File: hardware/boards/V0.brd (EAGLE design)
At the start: 61 parts, among them IC2 TPS6300, J1 SJ-43515TS-SMT, J2 HIROSE_DM3BT-DSF-PEJSHIROSE_D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, J3 MOLEX_105450-0101MOLEX_105450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, Q1 MC-306, Q2 ON_SEMI_MMBT5551LT1GON_SEMI_M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, U1 VS1053-L, X1 PG203J, X3 FH12-45S-0.5SH

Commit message: checkpoint: USB
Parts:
- added C21: 0.1uF, rcl:C0805K
- added C22, C24: 4.7uF, rcl:C/6032-28R
- added C23, C25: 0.1uF, rcl:C/6032-28R
- added CENTER_SW, DOWN_SW, LEFT_SW, RIGHT_SW, UP_SW: E-SWITCH_TL3315NF160QE-SWITCH_TL3315NF160Q_0_0, E-Switch-TL3315NF160Q:E-SWITCH_TL3315NF160Q_0
- added D10, D8, D9: ON_SEMICONDUCTOR_ESD5Z5.0T1GON_SEMICONDUCTOR_ESD5Z5.0T1G_0_0, ESD-Diode_On-Semi-ESD5Z5.0T1G:ON_SEMICONDUCTOR_ESD5Z5.0T1G_0
- added D3, D4, D5, D6, D7: (no value), adafruit:SOD-523
- added R19, R25, R33: 5k, rcl:R0805
- added R20: 15k, rcl:R0805
- added R21: 35k, rcl:R0805
- added R22: 75k, rcl:R0805
- added R23: 155k, rcl:R0805
- added R24: 50k, rcl:R0805
- added R26, R32: 10k, rcl:R0805
- added R27, R28: 5.1k, rcl:R0805
- added R29: 22.1k, rcl:R0805
- added R30: 47.5k, rcl:R0805
- added R31: 1k, rcl:R0805
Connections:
- removed net 1_GND: J3.A1
- removed net 1_VBUS: J3.A4
- removed net 2_GND: J3.A12
- removed net 2_VBUS: J3.A9
- removed net 3_GND: J3.B1
- removed net 3_VBUS: J3.B4
- removed net 4_GND: J3.B12
- removed net 4_VBUS: J3.B9
- removed net VDD: JL.P$6
- removed net VREGIN: JL.P$7
- new net BUTTON_ADC: R19.1, R20.1, R21.1, R22.1, R23.1, R25.2
- new net BUTTON_DIN: C21.2, R24.2
- new net CP_VDD: C24.+, C25.+, JL.P$6, R31.2
- new net N$16: D3.A, LEFT_SW.4, LEFT_SW.4-2, R19.2
- new net N$24: D4.A, R20.2, UP_SW.4, UP_SW.4-2
- new net N$28: D5.A, R21.2, RIGHT_SW.4, RIGHT_SW.4-2
- new net N$29: D6.A, DOWN_SW.4, DOWN_SW.4-2, R22.2
- new net N$32: D3.K, D4.K, D5.K, D6.K, D7.K, R24.1, R26.2
- new net N$49: CENTER_SW.4, CENTER_SW.4-2, D7.A, R23.2
- new net N$50: J3.A5, R27.1
- new net N$51: J3.B5, R28.1
- new net N$52: JL.P$8, R29.1, R30.2
- new net N$53: JL.P$9, R31.1
- new net USB_D+: D9.1, J3.A6, J3.B6, JL.P$4
- new net USB_D-: D8.1, J3.A7, J3.B7, JL.P$5
- new net VBAT_ADC_IN: R32.2, R33.1
- new net VBUS: D10.1, J3.A4, J3.A9, J3.B4, J3.B9, R29.2
- net GND: now also C22.-, C23.-, C24.-, C25.-, D10.2, D8.2, D9.2, J3.1, J3.2, J3.3, J3.4, J3.A1, J3.A12, J3.B1, J3.B12, R25.1, R26.1, R27.2, R28.2, R30.1, R32.1
- net V3P3: now also C21.1, CENTER_SW.2, CENTER_SW.2-2, D1.2, DOWN_SW.2, DOWN_SW.2-2, LEFT_SW.2, LEFT_SW.2-2, RIGHT_SW.2, RIGHT_SW.2-2, UP_SW.2, UP_SW.2-2
- net VBAT: now also C22.+, C23.+, JL.P$7, R33.2

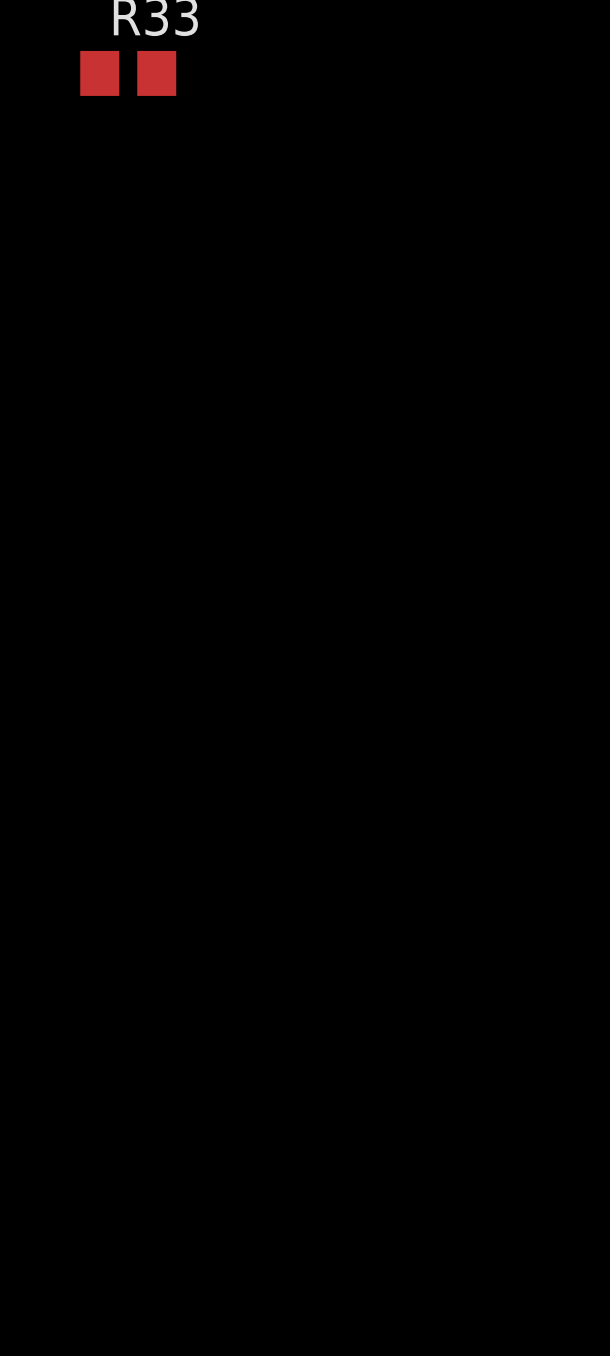
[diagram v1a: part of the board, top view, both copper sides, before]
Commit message: checkpoint: LED, battery voltage circuit, charge IC, half of the CP2102N
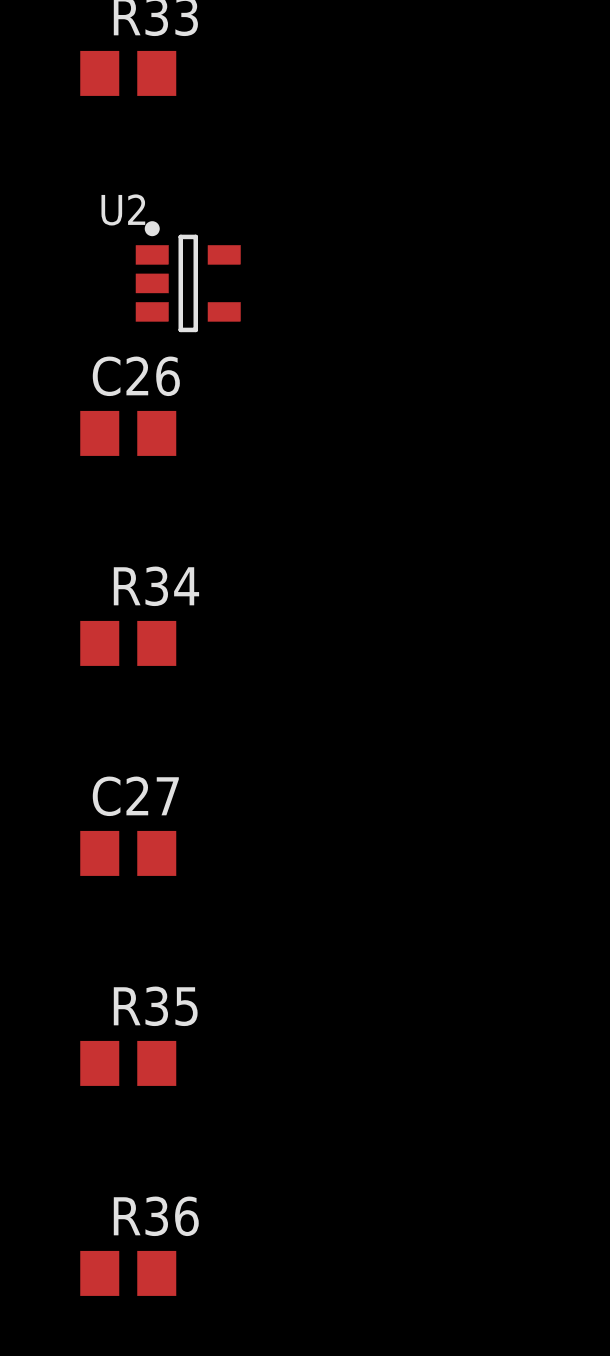
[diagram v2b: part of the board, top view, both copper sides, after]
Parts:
- added C26, C27: 4.7uF, rcl:C0805
- added R34: 2k, rcl:R0805
- added R35: 100, rcl:R0805
- added R36: (no value), rcl:R0805
- added U2: MICROCHIP_MCP73831T-2ATI-OTMICROCHIP_MCP73831T-2ATI-OT_0_1, Microchip-MCP73831T-2ATI:MICROCHIP_MCP73831T-2ATI-OT_1
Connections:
- new net BLUE_LED_CATH: D1.1
- new net GREEN_LED_CATH: R36.2
- new net N$54: R34.1, U2.5
- new net N$55: D1.3, R35.1
- new net N$56: D1.4, R36.1
- new net RED_LED_CATH: R35.2, U2.1
- net GND: now also C26.2, C27.2, R34.2, U2.2
- net VBAT: now also C26.1, U2.3
- net VBUS: now also C27.1, U2.4
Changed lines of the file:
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@@
 <attribute name="VALUE" x="-36.635" y="-531.54" size="1.27" layer="27"/>
+</element>
+<element name="U2" library="Microchip-MCP73831T-2ATI" package="MICROCHIP_MCP73831T-2ATI-OT_1" value="MICROCHIP_MCP73831T-2ATI-OTMICROCHIP_MCP73831T-2ATI-OT_0_1" x="-34" y="-536" smashed="yes">
+<attribute name="CIIVA_IDS" value="961386" x="-34" y="-536" size="1.778" layer="27" display="off"/>
+<attribute name="CODE__IPC" value="SOT23-5" x="-34" y="-536" size="1.778" layer="27" display="off"/>
+<attribute name="DATASHEET_VERSION" value="revE, Sep-2008" x="-34" y="-536" size="1.778" layer="27" display="off"/>
+<attribute name="FOOTPRINT_VARIANT_NAME_0" value="Level C" x="-34" y="-536" size="1.778" layer="27" display="off"/>
+<attribute name="FOOTPRINT_VARIANT_NAME_1" value="Level B" x="-34" y="-536" size="1.778" layer="27" display="off"/>
+<attribute name="FOOTPRINT_VARIANT_NAME_2" value="Level A" x="-34" y="-536" size="1.778" layer="27" display="off"/>
+<attribute name="IMPORTED" value="yes" x="-34" y="-536" size="1.778" layer="27" display="off"/>
+<attribute name="IMPORTED_FROM" value="vault" x="-34" y="-536" size="1.778" layer="27" display="off"/>
+<attribute name="IMPORT_TS" value="1521858219" x="-34" y="-536" size="1.778" layer="27" display="off"/>
+<attribute name="MF" value="Microchip" x="-34" y="-536" size="1.778" layer="27" display="off"/>
+<attribute name="MPN" value="MCP73831T-2ATI/OT" x="-34" y="-536" size="1.778" layer="27" display="off"/>
+<attribute name="NAME" x="-37" y="-534.05" size="1" layer="25"/>
+<attribute name="PACKAGE" value="SOT-23-OT5" x="-34" y="-536" size="1.778" layer="27" display="off"/>
+<attribute name="PACKAGE_DESCRIPTION" value="5-Lead Plastic Small Outline Transistor (OT) [SOT-23]" x="-34" y="-536" size="1.778" layer="27" display="off"/>
+<attribute name="PACKAGE_VERSION" value="revBB, Aug-2009" x="-34" y="-536" size="1.778" layer="27" display="off"/>
+<attribute name="PREFIX" value="U" x="-34" y="-536" size="1.778" layer="27" display="off"/>
+<attribute name="RELEASE_DATE" value="1300334172" x="-34" y="-536" size="1.778" layer="27" display="off"/>
+<attribute name="VAULT_GUID" value="2E16BB74-376E-4BA5-8468-379BB32F6F4F" x="-34" y="-536" size="1.778" layer="27" display="off"/>
+<attribute name="VAULT_REVISION" value="08CA403F-6CAA-4AD2-9BA5-F14A59377F17" x="-34" y="-536" size="1.778" layer="27" display="off"/>
+</element>
+<element name="C26" library="rcl" library_urn="urn:adsk.eagle:library:334" package="C0805" package3d_urn="urn:adsk.eagle:package:23617/2" value="4.7uF" x="-36" y="-541" smashed="yes">
+<attribute name="NAME" x="-37.27" y="-539.73" size="1.27" layer="25"/>
+<attribute name="SPICEPREFIX" value="C" x="-36" y="-541" size="1.778" layer="27" display="off"/>
+<attribute name="VALUE" x="-37.27" y="-543.54" size="1.27" layer="27"/>
+</element>
+<element name="R34" library="rcl" library_urn="urn:adsk.eagle:library:334" package="R0805" package3d_urn="urn:adsk.eagle:package:23553/2" value="2k" x="-36" y="-548" smashed="yes">
+<attribute name="NAME" x="-36.635" y="-546.73" size="1.27" layer="25"/>
+<attribute name="SPICEPREFIX" value="R" x="-36" y="-548" size="1.778" layer="27" display="off"/>
+<attribute name="VALUE" x="-36.635" y="-550.54" size="1.27" layer="27"/>
+</element>
+<element name="C27" library="rcl" library_urn="urn:adsk.eagle:library:334" package="C0805" package3d_urn="urn:adsk.eagle:package:23617/2" value="4.7uF" x="-36" y="-555" smashed="yes">
+<attribute name="NAME" x="-37.27" y="-553.73" size="1.27" layer="25"/>
+<attribute name="SPICEPREFIX" value="C" x="-36" y="-555" size="1.778" layer="27" display="off"/>
+<attribute name="VALUE" x="-37.27" y="-557.54" size="1.27" layer="27"/>
+</element>
+<element name="R35" library="rcl" library_urn="urn:adsk.eagle:library:334" package="R0805" package3d_urn="urn:adsk.eagle:package:23553/2" value="100" x="-36" y="-562" smashed="yes">
+<attribute name="NAME" x="-36.635" y="-560.73" size="1.27" layer="25"/>
+<attribute name="SPICEPREFIX" value="R" x="-36" y="-562" size="1.778" layer="27" display="off"/>
+<attribute name="VALUE" x="-36.635" y="-564.54" size="1.27" layer="27"/>
+</element>
+<element name="R36" library="rcl" library_urn="urn:adsk.eagle:library:334" package="R0805" package3d_urn="urn:adsk.eagle:package:23553/2" value="" x="-36" y="-569" smashed="yes">
+<attribute name="NAME" x="-36.635" y="-567.73" size="1.27" layer="25"/>
+<attribute name="SPICEPREFIX" value="R" x="-36" y="-569" size="1.778" layer="27" display="off"/>
+<attribute name="VALUE" x="-36.635" y="-571.54" size="1.27" layer="27"/>
 </element>
 </elements>
@@
 <contactref element="C25" pad="-"/>
 <contactref element="R32" pad="1"/>
+<contactref element="C26" pad="2"/>
+<contactref element="U2" pad="2"/>
+<contactref element="R34" pad="2"/>
+<contactref element="C27" pad="2"/>
 <wire x1="-21.275" y1="-222.175" x2="-28.675" y2="-222.175" width="0" layer="19" extent="1-1"/>
 <wire x1="-24.075" y1="-200.0822" x2="-21.275" y2="-222.175" width="0" layer="19" extent="1-1"/>
@@
 <wire x1="-36.525" y1="-517" x2="-36.525" y2="-509" width="0" layer="19" extent="1-1"/>
 <wire x1="-36.95" y1="-524" x2="-36.525" y2="-517" width="0" layer="19" extent="1-1"/>
+<wire x1="-35.2" y1="-536" x2="-36.95" y2="-524" width="0" layer="19" extent="1-1"/>
+<wire x1="-35.05" y1="-541" x2="-35.2" y2="-536" width="0" layer="19" extent="1-1"/>
+<wire x1="-35.05" y1="-548" x2="-35.05" y2="-541" width="0" layer="19" extent="1-1"/>
+<wire x1="-35.05" y1="-555" x2="-35.05" y2="-548" width="0" layer="19" extent="1-1"/>
 <wire x1="-18" y1="-7" x2="-19" y2="-82.95" width="0" layer="19" extent="1-1"/>
 <wire x1="-24.135" y1="0.35" x2="-18" y2="-7" width="0" layer="19" extent="1-1"/>
@@
 <contactref element="C23" pad="+"/>
 <contactref element="R33" pad="2"/>
+<contactref element="U2" pad="3"/>
+<contactref element="C26" pad="1"/>
 <wire x1="-18.8375" y1="-156" x2="-27.5" y2="-162.95" width="0" layer="19" extent="1-1"/>
 <wire x1="-24.85" y1="-150" x2="-18.8375" y2="-156" width="0" layer="19" extent="1-1"/>
@@
 <wire x1="-31.475" y1="-501" x2="-31.475" y2="-495" width="0" layer="19" extent="1-1"/>
 <wire x1="-35.05" y1="-529" x2="-31.475" y2="-501" width="0" layer="19" extent="1-1"/>
+<wire x1="-35.2" y1="-536.95" x2="-35.05" y2="-529" width="0" layer="19" extent="1-1"/>
+<wire x1="-36.95" y1="-541" x2="-35.2" y2="-536.95" width="0" layer="19" extent="1-1"/>
 </signal>
 <signal name="V3P3">
@@
 <contactref element="D10" pad="1"/>
 <contactref element="R29" pad="2"/>
+<contactref element="C27" pad="1"/>
+<contactref element="U2" pad="4"/>
 <wire x1="-35.05" y1="-476" x2="-35.66" y2="-459" width="0" layer="19" extent="1-1"/>
+<wire x1="-32.8" y1="-536.95" x2="-35.05" y2="-476" width="0" layer="19" extent="1-1"/>
+<wire x1="-36.95" y1="-555" x2="-32.8" y2="-536.95" width="0" layer="19" extent="1-1"/>
 <wire x1="-27.25" y1="-341.53" x2="-35.66" y2="-459" width="0" layer="19" extent="1-1"/>
 <wire x1="-27.5" y1="-340.23" x2="-27.25" y2="-341.53" width="0" layer="19" extent="1-1"/>
@@
 <wire x1="-35.05" y1="-524" x2="-36.95" y2="-529" width="0" layer="19" extent="1-1"/>
 </signal>
+<signal name="N$54">
+<contactref element="U2" pad="5"/>
+<contactref element="R34" pad="1"/>
+<wire x1="-32.8" y1="-535.05" x2="-36.95" y2="-548" width="0" layer="19" extent="1-1"/>
+</signal>
+<signal name="N$55">
+<contactref element="D1" pad="3"/>
+<contactref element="R35" pad="1"/>
+<wire x1="-36.95" y1="-562" x2="-28.575" y2="-351.6" width="0" layer="19" extent="1-1"/>
+</signal>
+<signal name="RED_LED_CATH">
+<contactref element="R35" pad="2"/>
+<contactref element="U2" pad="1"/>
+<wire x1="-35.2" y1="-535.05" x2="-35.05" y2="-562" width="0" layer="19" extent="1-1"/>
+</signal>
+<signal name="N$56">
+<contactref element="D1" pad="4"/>
+<contactref element="R36" pad="1"/>
+<wire x1="-36.95" y1="-569" x2="-27.675" y2="-351.25" width="0" layer="19" extent="1-1"/>
+</signal>
+<signal name="GREEN_LED_CATH">
+<contactref element="R36" pad="2"/>
+</signal>
+<signal name="BLUE_LED_CATH">
+<contactref element="D1" pad="1"/>
+</signal>
 </signals>

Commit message: checkpoint: power on and off circuit
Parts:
- removed SW1: (no value), adafruit:PUSHBUTTON_SMD_SJ
- added CENTER_SW_PWR: E-SWITCH_TL3315NF160QE-SWITCH_TL3315NF160Q_0_0, E-Switch-TL3315NF160Q:E-SWITCH_TL3315NF160Q_0
- C6, C7: device adafruit:C025-024X044 -> rcl:C1206
- R10, R9: device adafruit:0204V -> rcl:R0805
- R11: device adafruit:R3216 -> rcl:R0805
- R19: value 5k -> 155k
- R20: value 15k -> 75k
- R22: value 75k -> 15k
- R23: value 155k -> 5k
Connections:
- net N$49 renamed CENTER_SW
- removed net N$11: R10.2, R9.2
- removed net N$18: U$2.3, U$2.5
- removed net N$20: U$2.14
- removed net N$21: U$2.13
- removed net N$23: R11.1, SW1.P$2
- new net CENTER_SW_PWR_BTM: CENTER_SW_PWR.4, CENTER_SW_PWR.4-2
- new net CENTER_SW_PWR_TOP: CENTER_SW_PWR.2, CENTER_SW_PWR.2-2, R11.1
- new net SYS_ENABLE: IC2.6, U$2.3, U$2.5
- net GND: now also U$2.13; no longer SW1.P$1
- net N$3: no longer IC2.6
- net VBAT: now also R10.2, R9.2, U$2.14

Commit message: misc VS1053 fixes + fix/wire ATQ
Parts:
- removed WHEEL_C: (no value), pinhead:1X03/90
- added C28, C29: 10uF, rcl:C/6032-28R
- added CH0, CH1, CH2, GUARD: TPSQTP20SQ, testpad:TP20SQ
- added R37, R38, R39: 4.7k, rcl:R0805
- added R40, R41, R42, R43: 10k, rcl:R0805
- C15, C16, C17, C18, C19, C20: value (none) -> 100nF
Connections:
- removed net +3V3: C15.1, C16.1, C17.1, U1.24, U1.31, U1.38, U1.43, U1.45, U1.5, U1.7
- removed net N$27 (its old number): U$6.7, WHEEL_C.1
- removed net N$48: U1.27
- removed net VCCIO: C18.1, C19.1, C20.1, R17.2, U1.14, U1.19, U1.32, U1.6
- new net ATQ_CHANGE: R39.1, U$6.17
- new net I2C_SCL: R38.1, U$6.16
- new net I2C_SDA: R37.1, U$6.13
- new net N$11: R40.1, U$6.9
- new net N$18: CH1.TP, R41.2
- new net N$20: CH2.TP, R42.2
- new net N$23: R41.1, U$6.8
- new net N$37: CH0.TP, R40.2
- new net N$40: GUARD.TP, R43.2
- net GND: now also C28.-, C29.-, U$6.10, U$6.12; no longer U$6.11
- net N$25: now also R42.1, U$6.7; no longer U$6.9, WHEEL_C.3
- net N$26: now also R43.1, U$6.6; no longer U$6.8, WHEEL_C.2
- net V1P8: now also C18.1, C19.1, C20.1, C28.+, U1.24, U1.31, U1.5, U1.7
- net V3P3: now also C15.1, C16.1, C17.1, C29.+, R17.2, R37.2, R38.2, R39.2, U$6.11, U1.14, U1.19, U1.32, U1.38, U1.43, U1.45, U1.6; no longer U$6.10, U$6.12

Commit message: inline + tip switch (bad) + ??
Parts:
- removed X1: PG203J, con-hirschmann:PG203J
- added R44: 10K, rcl:R0805
- added R45: 50k, rcl:R0805
- C12: value 10nF -> 47nF
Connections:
- removed net N$30: R13.1, U1.42, X1.2
- removed net N$31: R14.1, U1.39, X1.1
- new net N$48: J1.4, R13.1, U1.42
- new net N$49: J1.3, R14.1, U1.39
- new net TRRS_INLINE_CTRL: J1.1, R44.1, U$1.11
- new net TRRS_TIP_SW: J1.5, R45.1, U$1.5
- net GND: now also R45.2; no longer X1.3, X1.4
- net N$33: now also J1.2; no longer X1.5
- net V3P3: now also R44.2
